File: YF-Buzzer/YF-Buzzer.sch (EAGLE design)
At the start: 6 parts, among them IC1 74HC595N, IC2 74HC595N, IC3 74HC595N, IC4 74HC595N, IC5 74HC595N, IC6 74HC595N

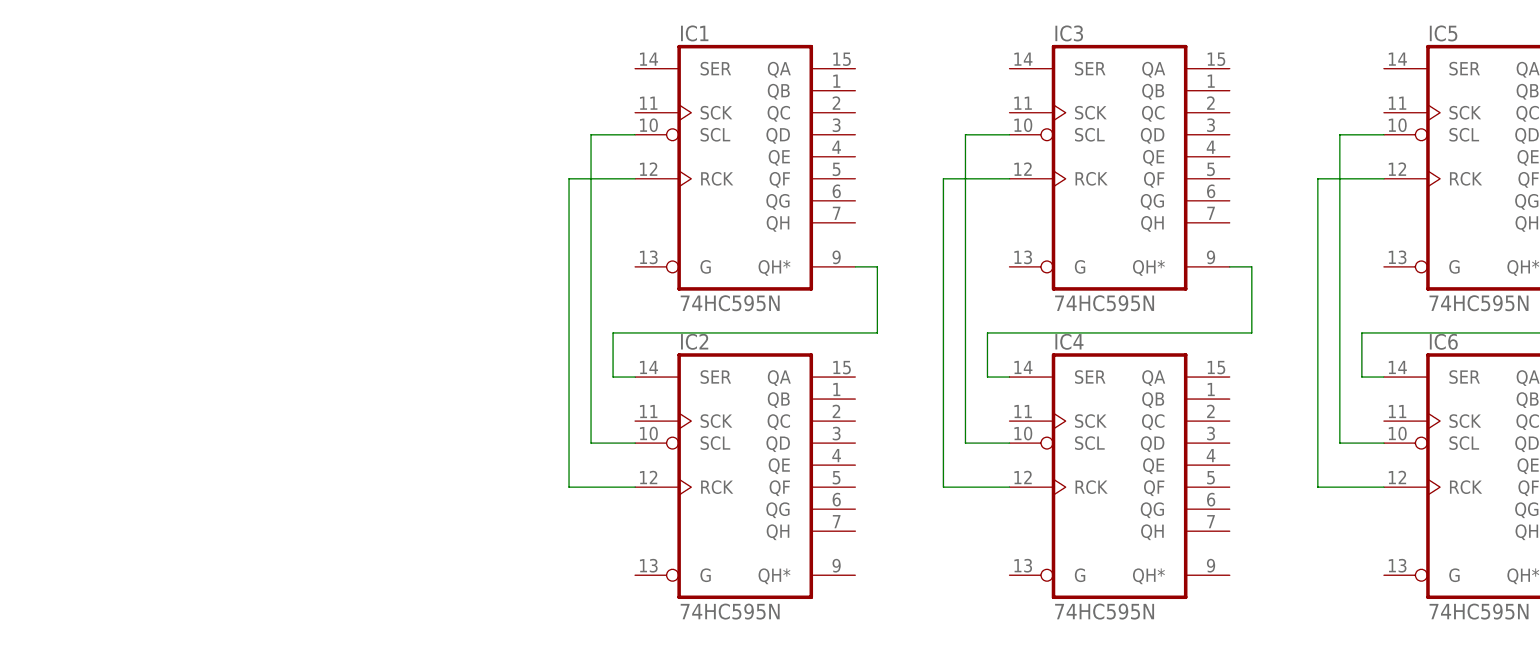
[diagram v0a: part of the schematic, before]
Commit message: Added code for shifting data into registers and reading the demux.
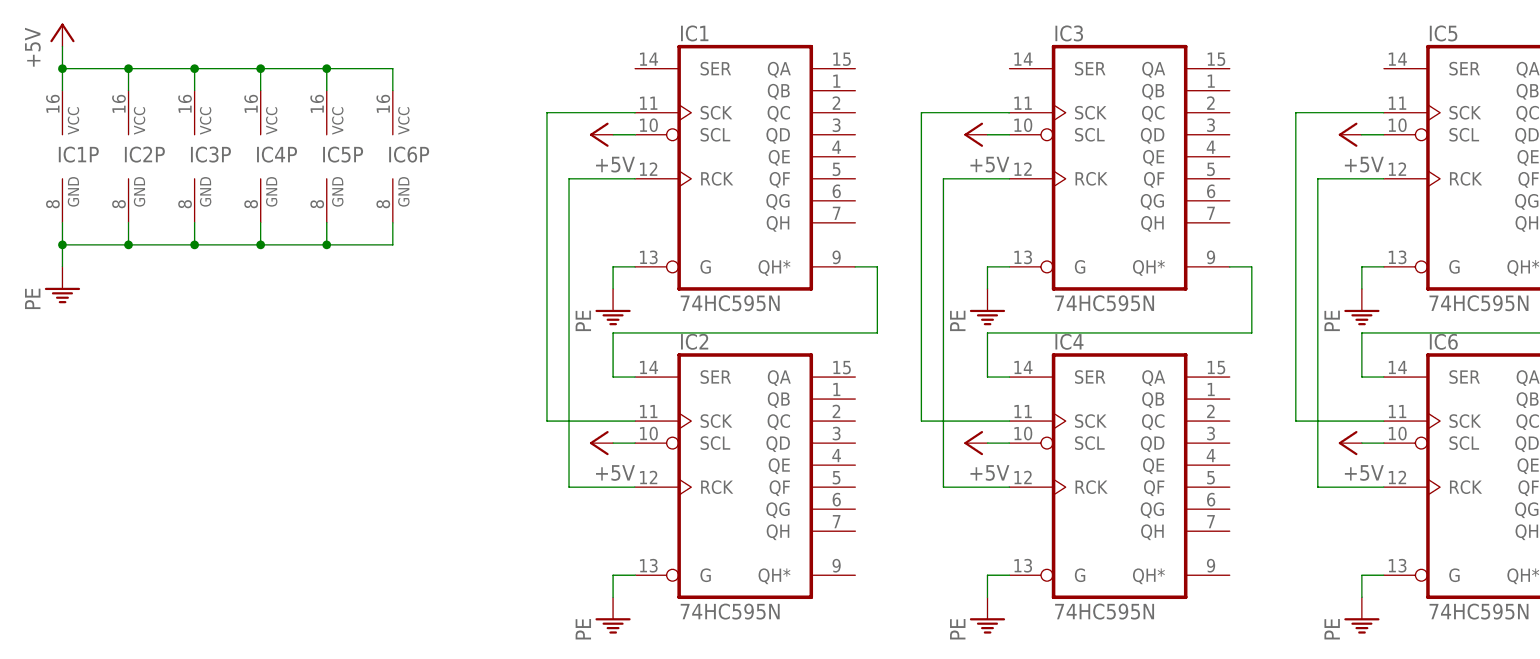
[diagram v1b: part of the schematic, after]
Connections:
- new net +5V: IC1A.SCL, IC1P.VCC, IC2A.SCL, IC2P.VCC, IC3A.SCL, IC3P.VCC, IC4A.SCL, IC4P.VCC, IC5A.SCL, IC5P.VCC, IC6A.SCL, IC6P.VCC
- new net PE: IC1A.G, IC1P.GND, IC2A.G, IC2P.GND, IC3A.G, IC3P.GND, IC4A.G, IC4P.GND, IC5A.G, IC5P.GND, IC6A.G, IC6P.GND
- net N$4: now also IC5A.SCK, IC6A.SCK; no longer IC1A.SCL, IC2A.SCL
- net N$6: now also IC3A.SCK, IC4A.SCK; no longer IC3A.SCL, IC4A.SCL
- net N$8: now also IC1A.SCK, IC2A.SCK; no longer IC5A.SCL, IC6A.SCL

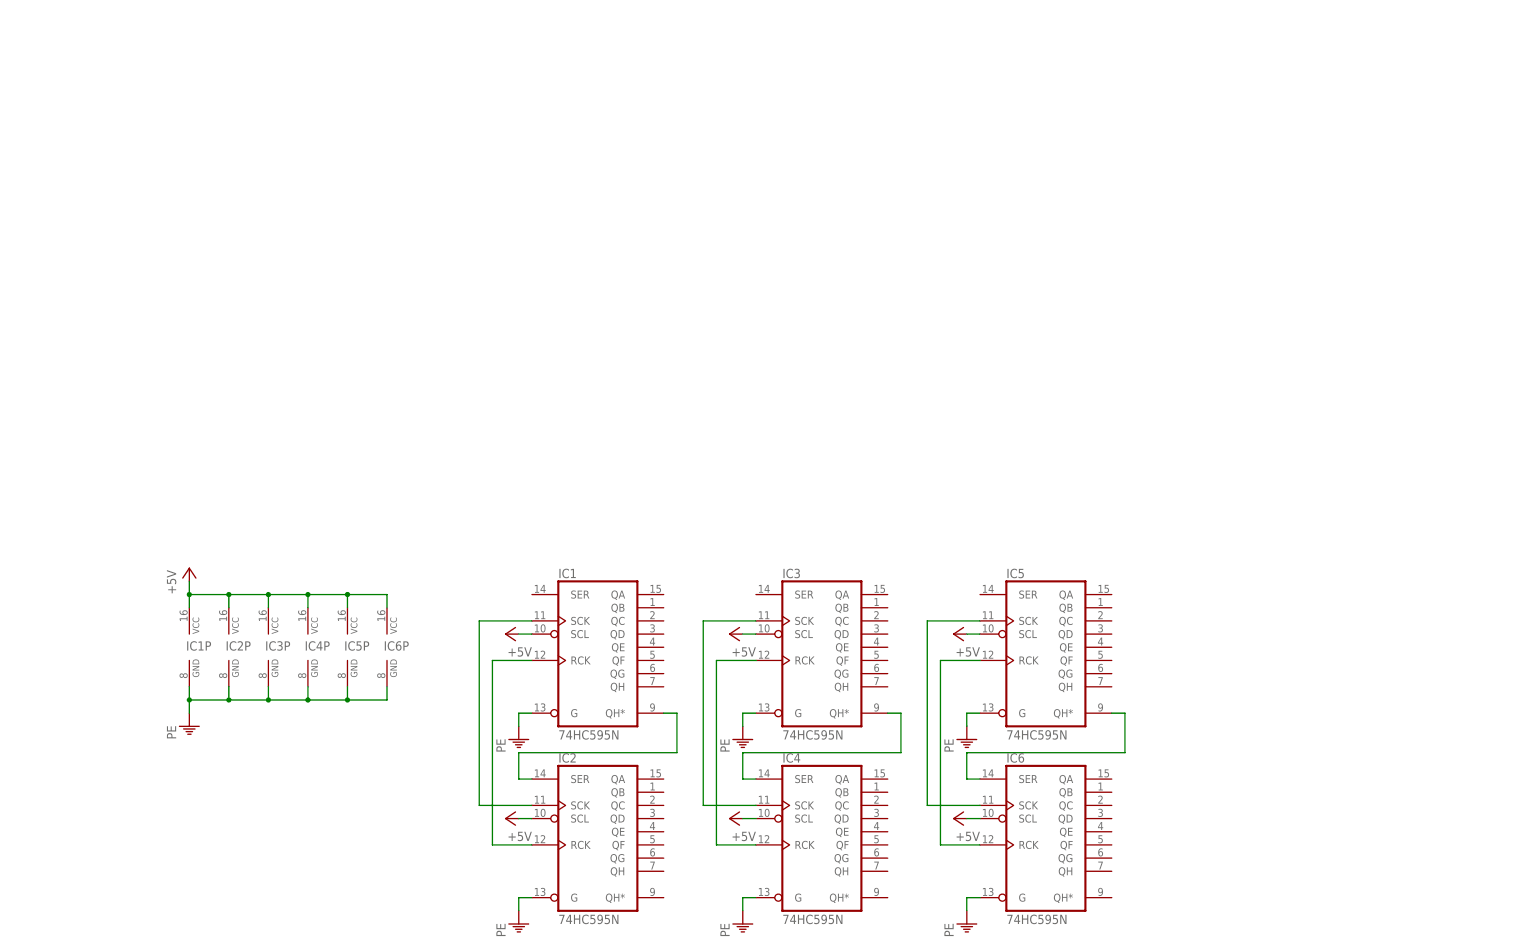
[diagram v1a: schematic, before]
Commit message: Added the multiplexer and microcontroller to the circuit.
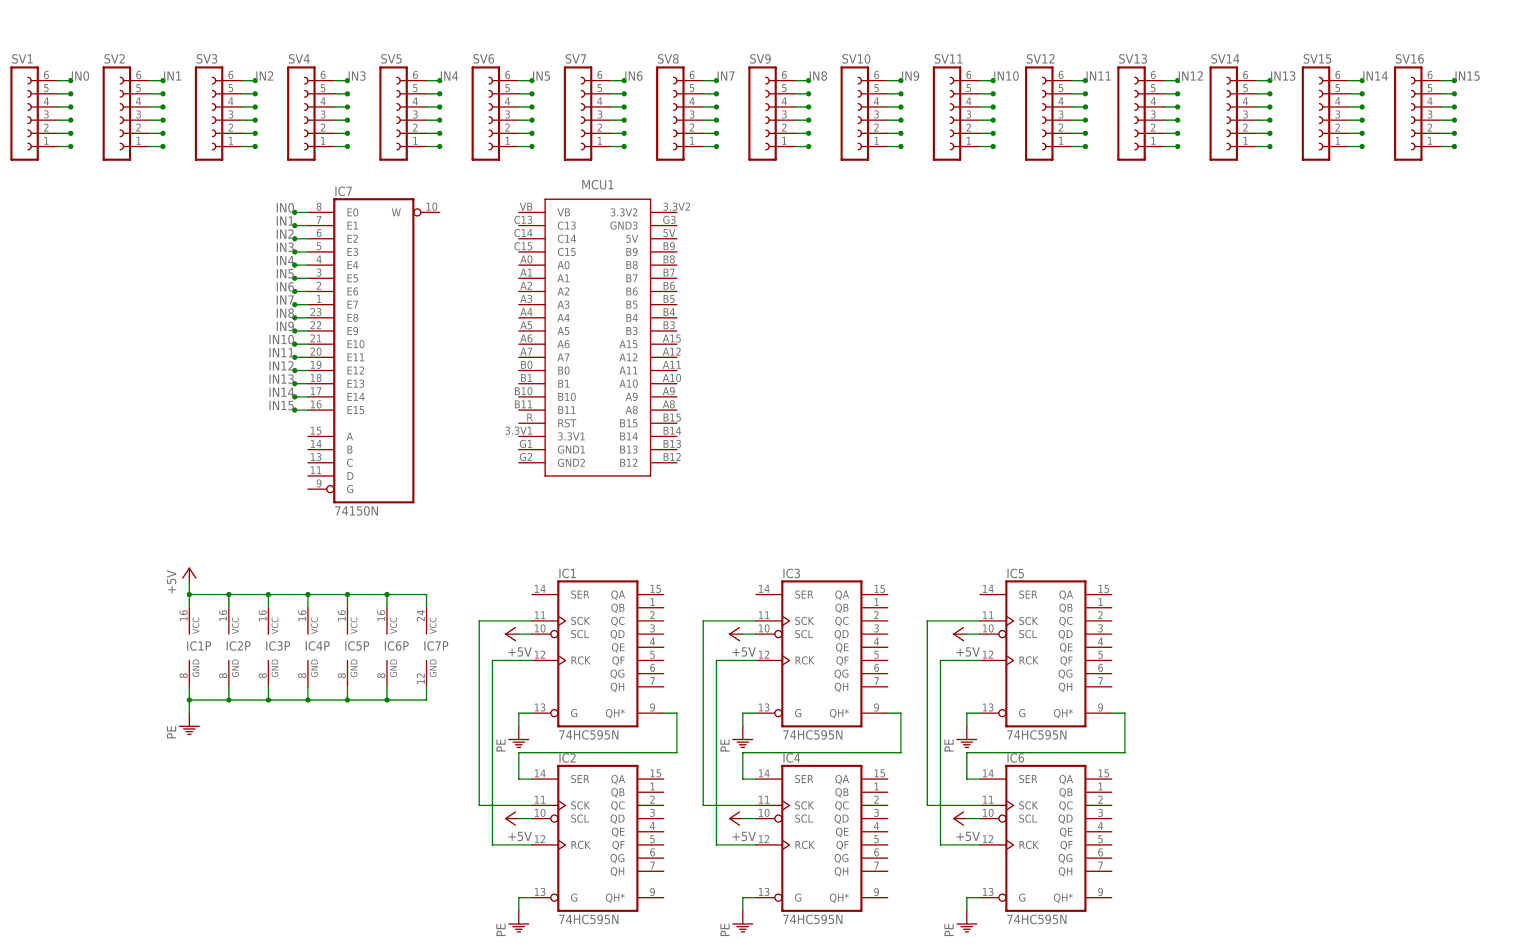
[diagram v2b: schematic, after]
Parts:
- added IC7: 74150N, 74xx-eu:74150N
- added MCU1: (no value), Jonathan:STM32-BLUE
- added SV1, SV10, SV11, SV12, SV13, SV14, SV15, SV16, SV2, SV3, SV4, SV5, SV6, SV7, SV8, SV9: (no value), con-lsta:FE06-1
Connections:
- new net IN0: IC7A.E0, SV1.6
- new net IN1: IC7A.E1, SV2.6
- new net IN10: IC7A.E10, SV11.6
- new net IN11: IC7A.E11, SV12.6
- new net IN12: IC7A.E12, SV13.6
- new net IN13: IC7A.E13, SV14.6
- new net IN14: IC7A.E14, SV15.6
- new net IN15: IC7A.E15, SV16.6
- new net IN2: IC7A.E2, SV3.6
- new net IN3: IC7A.E3, SV4.6
- new net IN4: IC7A.E4, SV5.6
- new net IN5: IC7A.E5, SV6.6
- new net IN6: IC7A.E6, SV7.6
- new net IN7: IC7A.E7, SV8.6
- new net IN8: IC7A.E8, SV9.6
- new net IN9: IC7A.E9, SV10.6
- new net N$10: SV2.5
- new net N$11: SV1.5
- new net N$12: SV1.4
- new net N$13: SV1.3
- new net N$14: SV1.2
- new net N$15: SV1.1
- new net N$16: SV5.5
- new net N$17: SV5.4
- new net N$18: SV2.4
- new net N$19: SV2.3
- new net N$20: SV2.2
- new net N$21: SV2.1
- new net N$22: SV3.5
- new net N$23: SV3.4
- new net N$24: SV3.3
- new net N$25: SV3.2
- new net N$26: SV3.1
- new net N$27: SV4.5
- new net N$28: SV4.4
- new net N$29: SV4.3
- new net N$30: SV4.2
- new net N$31: SV4.1
- new net N$32: SV5.3
- new net N$33: SV5.2
- new net N$34: SV5.1
- new net N$35: SV6.5
- new net N$36: SV6.4
- new net N$37: SV6.3
- new net N$38: SV6.2
- new net N$39: SV6.1
- new net N$40: SV7.5
- new net N$41: SV7.4
- new net N$42: SV7.3
- new net N$43: SV7.2
- new net N$44: SV7.1
- new net N$45: SV8.5
- new net N$46: SV8.4
- new net N$47: SV8.3
- new net N$48: SV8.2
- new net N$49: SV8.1
- new net N$50: SV9.5
- new net N$51: SV9.4
- new net N$52: SV9.3
- new net N$53: SV9.2
- new net N$54: SV9.1
- new net N$55: SV10.5
- new net N$56: SV10.4
- new net N$57: SV10.3
- new net N$58: SV10.2
- new net N$59: SV10.1
- new net N$60: SV11.5
- new net N$61: SV11.4
- new net N$62: SV11.3
- new net N$63: SV11.2
- new net N$64: SV11.1
- new net N$65: SV12.5
- new net N$66: SV12.4
- new net N$67: SV12.3
- new net N$68: SV12.2
- new net N$69: SV12.1
- new net N$70: SV13.5
- new net N$71: SV13.4
- new net N$72: SV13.3
- new net N$73: SV13.2
- new net N$74: SV13.1
- new net N$75: SV14.5
- new net N$76: SV14.4
- new net N$77: SV14.3
- new net N$78: SV14.2
- new net N$79: SV14.1
- new net N$80: SV15.5
- new net N$81: SV15.4
- new net N$82: SV15.3
- new net N$83: SV15.2
- new net N$84: SV15.1
- new net N$85: SV16.5
- new net N$86: SV16.4
- new net N$87: SV16.3
- new net N$88: SV16.2
- new net N$89: SV16.1
- net +5V: now also IC7P.VCC
- net PE: now also IC7P.GND

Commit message: Finished the shift register circuits and began layout of the PCB.
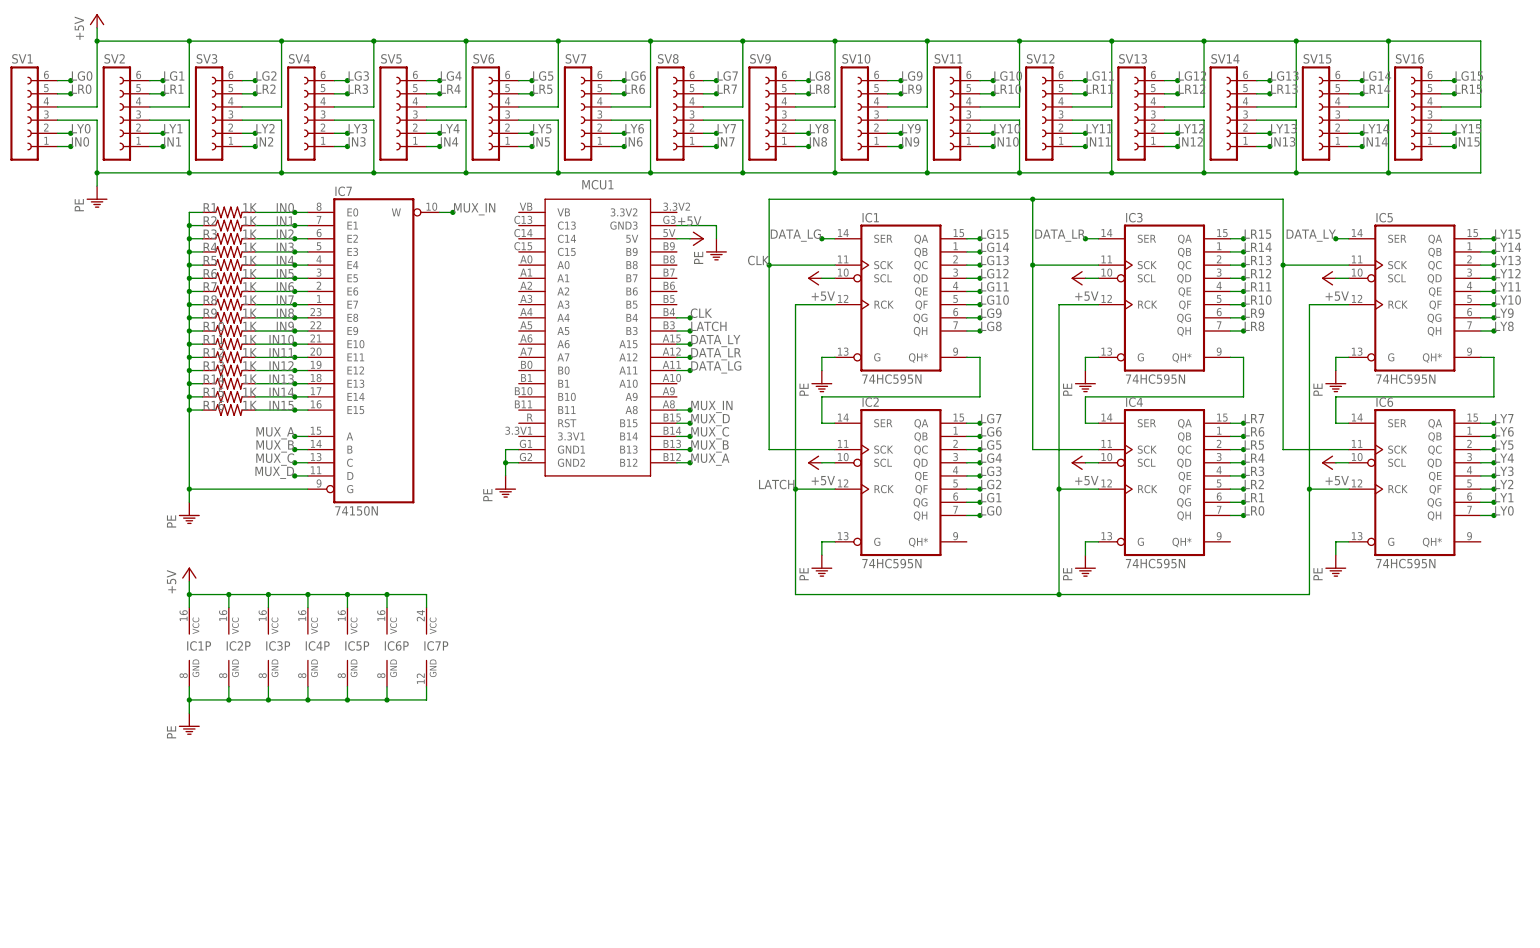
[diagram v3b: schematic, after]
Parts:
- added R1, R10, R11, R12, R13, R14, R15, R16, R2, R3, R4, R5, R6, R7, R8, R9: 1K, rcl:R-US_0207/10
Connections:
- removed net N$10: SV2.5
- removed net N$11: SV1.5
- removed net N$12: SV1.4
- removed net N$13: SV1.3
- removed net N$14: SV1.2
- removed net N$15: SV1.1
- removed net N$16: SV5.5
- removed net N$17: SV5.4
- removed net N$18: SV2.4
- removed net N$19: SV2.3
- removed net N$20: SV2.2
- removed net N$21: SV2.1
- removed net N$22: SV3.5
- removed net N$23: SV3.4
- removed net N$24: SV3.3
- removed net N$25: SV3.2
- removed net N$26: SV3.1
- removed net N$27: SV4.5
- removed net N$28: SV4.4
- removed net N$29: SV4.3
- removed net N$30: SV4.2
- removed net N$31: SV4.1
- removed net N$32: SV5.3
- removed net N$33: SV5.2
- removed net N$34: SV5.1
- removed net N$35: SV6.5
- removed net N$36: SV6.4
- removed net N$37: SV6.3
- removed net N$38: SV6.2
- removed net N$39: SV6.1
- removed net N$4: IC5A.SCK, IC6A.SCK
- removed net N$40: SV7.5
- removed net N$41: SV7.4
- removed net N$42: SV7.3
- removed net N$43: SV7.2
- removed net N$44: SV7.1
- removed net N$45: SV8.5
- removed net N$46: SV8.4
- removed net N$47: SV8.3
- removed net N$48: SV8.2
- removed net N$49: SV8.1
- removed net N$5: IC1A.RCK, IC2A.RCK
- removed net N$50: SV9.5
- removed net N$51: SV9.4
- removed net N$52: SV9.3
- removed net N$53: SV9.2
- removed net N$54: SV9.1
- removed net N$55: SV10.5
- removed net N$56: SV10.4
- removed net N$57: SV10.3
- removed net N$58: SV10.2
- removed net N$59: SV10.1
- removed net N$6: IC3A.SCK, IC4A.SCK
- removed net N$60: SV11.5
- removed net N$61: SV11.4
- removed net N$62: SV11.3
- removed net N$63: SV11.2
- removed net N$64: SV11.1
- removed net N$65: SV12.5
- removed net N$66: SV12.4
- removed net N$67: SV12.3
- removed net N$68: SV12.2
- removed net N$69: SV12.1
- removed net N$7: IC3A.RCK, IC4A.RCK
- removed net N$70: SV13.5
- removed net N$71: SV13.4
- removed net N$72: SV13.3
- removed net N$73: SV13.2
- removed net N$74: SV13.1
- removed net N$75: SV14.5
- removed net N$76: SV14.4
- removed net N$77: SV14.3
- removed net N$78: SV14.2
- removed net N$79: SV14.1
- removed net N$8: IC1A.SCK, IC2A.SCK
- removed net N$80: SV15.5
- removed net N$81: SV15.4
- removed net N$82: SV15.3
- removed net N$83: SV15.2
- removed net N$84: SV15.1
- removed net N$85: SV16.5
- removed net N$86: SV16.4
- removed net N$87: SV16.3
- removed net N$88: SV16.2
- removed net N$89: SV16.1
- removed net N$9: IC5A.RCK, IC6A.RCK
- new net CLK: IC1A.SCK, IC2A.SCK, IC3A.SCK, IC4A.SCK, IC5A.SCK, IC6A.SCK, MCU1.B4
- new net DATA_LG: IC1A.SER, MCU1.A11
- new net DATA_LR: IC3A.SER, MCU1.A12
- new net DATA_LY: IC5A.SER, MCU1.A15
- new net LATCH: IC1A.RCK, IC2A.RCK, IC3A.RCK, IC4A.RCK, IC5A.RCK, IC6A.RCK, MCU1.B3
- new net LG0: IC2A.QH, SV1.6
- new net LG1: IC2A.QG, SV2.6
- new net LG10: IC1A.QF, SV11.6
- new net LG11: IC1A.QE, SV12.6
- new net LG12: IC1A.QD, SV13.6
- new net LG13: IC1A.QC, SV14.6
- new net LG14: IC1A.QB, SV15.6
- new net LG15: IC1A.QA, SV16.6
- new net LG2: IC2A.QF, SV3.6
- new net LG3: IC2A.QE, SV4.6
- new net LG4: IC2A.QD, SV5.6
- new net LG5: IC2A.QC, SV6.6
- new net LG6: IC2A.QB, SV7.6
- new net LG7: IC2A.QA, SV8.6
- new net LG8: IC1A.QH, SV9.6
- new net LG9: IC1A.QG, SV10.6
- new net LR0: IC4A.QH, SV1.5
- new net LR1: IC4A.QG, SV2.5
- new net LR10: IC3A.QF, SV11.5
- new net LR11: IC3A.QE, SV12.5
- new net LR12: IC3A.QD, SV13.5
- new net LR13: IC3A.QC, SV14.5
- new net LR14: IC3A.QB, SV15.5
- new net LR15: IC3A.QA, SV16.5
- new net LR2: IC4A.QF, SV3.5
- new net LR3: IC4A.QE, SV4.5
- new net LR4: IC4A.QD, SV5.5
- new net LR5: IC4A.QC, SV6.5
- new net LR6: IC4A.QB, SV7.5
- new net LR7: IC4A.QA, SV8.5
- new net LR8: IC3A.QH, SV9.5
- new net LR9: IC3A.QG, SV10.5
- new net LY0: IC6A.QH, SV1.2
- new net LY1: IC6A.QG, SV2.2
- new net LY10: IC5A.QF, SV11.2
- new net LY11: IC5A.QE, SV12.2
- new net LY12: IC5A.QD, SV13.2
- new net LY13: IC5A.QC, SV14.2
- new net LY14: IC5A.QB, SV15.2
- new net LY15: IC5A.QA, SV16.2
- new net LY2: IC6A.QF, SV3.2
- new net LY3: IC6A.QE, SV4.2
- new net LY4: IC6A.QD, SV5.2
- new net LY5: IC6A.QC, SV6.2
- new net LY6: IC6A.QB, SV7.2
- new net LY7: IC6A.QA, SV8.2
- new net LY8: IC5A.QH, SV9.2
- new net LY9: IC5A.QG, SV10.2
- new net MUX_A: IC7A.A, MCU1.B12
- new net MUX_B: IC7A.B, MCU1.B13
- new net MUX_C: IC7A.C, MCU1.B14
- new net MUX_D: IC7A.D, MCU1.B15
- new net MUX_IN: IC7A.W, MCU1.A8
- net +5V: now also MCU1.5V, SV1.4, SV10.4, SV11.4, SV12.4, SV13.4, SV14.4, SV15.4, SV16.4, SV2.4, SV3.4, SV4.4, SV5.4, SV6.4, SV7.4, SV8.4, SV9.4
- net IN0: now also R1.2, SV1.1; no longer SV1.6
- net IN1: now also R2.2, SV2.1; no longer SV2.6
- net IN10: now also R11.2, SV11.1; no longer SV11.6
- net IN11: now also R12.2, SV12.1; no longer SV12.6
- net IN12: now also R13.2, SV13.1; no longer SV13.6
- net IN13: now also R14.2, SV14.1; no longer SV14.6
- net IN14: now also R15.2, SV15.1; no longer SV15.6
- net IN15: now also R16.2, SV16.1; no longer SV16.6
- net IN2: now also R3.2, SV3.1; no longer SV3.6
- net IN3: now also R4.2, SV4.1; no longer SV4.6
- net IN4: now also R5.2, SV5.1; no longer SV5.6
- net IN5: now also R6.2, SV6.1; no longer SV6.6
- net IN6: now also R7.2, SV7.1; no longer SV7.6
- net IN7: now also R8.2, SV8.1; no longer SV8.6
- net IN8: now also R9.2, SV9.1; no longer SV9.6
- net IN9: now also R10.2, SV10.1; no longer SV10.6
- net PE: now also IC7A.G, MCU1.GND1, MCU1.GND2, MCU1.GND3, R1.1, R10.1, R11.1, R12.1, R13.1, R14.1, R15.1, R16.1, R2.1, R3.1, R4.1, R5.1, R6.1, R7.1, R8.1, R9.1, SV1.3, SV10.3, SV11.3, SV12.3, SV13.3, SV14.3, SV15.3, SV16.3, SV2.3, SV3.3, SV4.3, SV5.3, SV6.3, SV7.3, SV8.3, SV9.3
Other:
- moved on the sheet: IC1, IC2, IC3, IC4, IC5, IC6
